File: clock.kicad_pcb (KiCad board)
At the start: 2 copper layers, 51.4 x 38.8 mm, 134 parts, among them J1 USB_C_Receptacle_USB2.0_16P, J3 Conn_01x02_Pin, J4 Conn_01x02_Pin, J5 Battery, Q1 2N7002K, Q2 NPN, SW1 SW_SPST, SW2 SW_SPST, SW4 SW_SPDT, SW5 SW_SPST, U1 STM32F072CBT6, U2 USBLC6-2SC6, U4 MCP73871-2CC, U5 AP2112K-3.3, Y1 8MHz

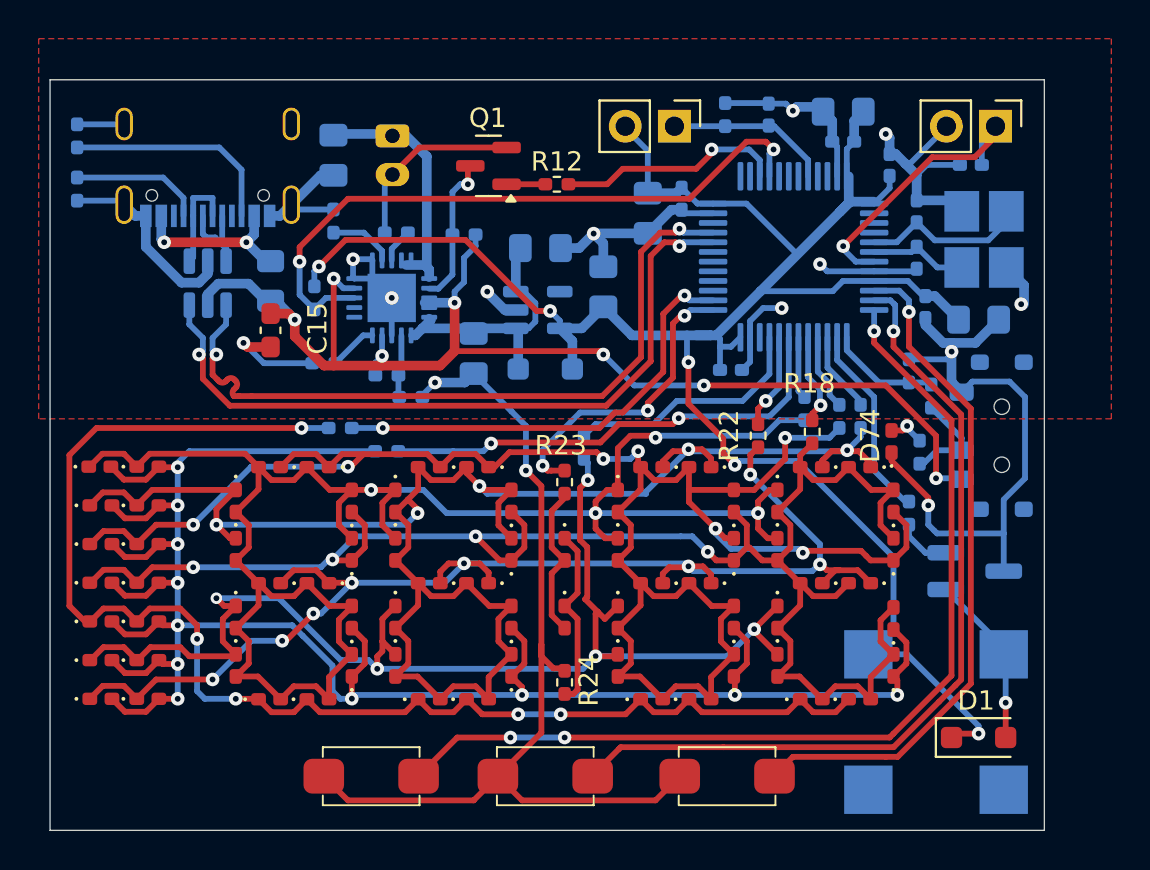
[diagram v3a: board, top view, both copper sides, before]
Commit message: fixed overlap of silkscreen
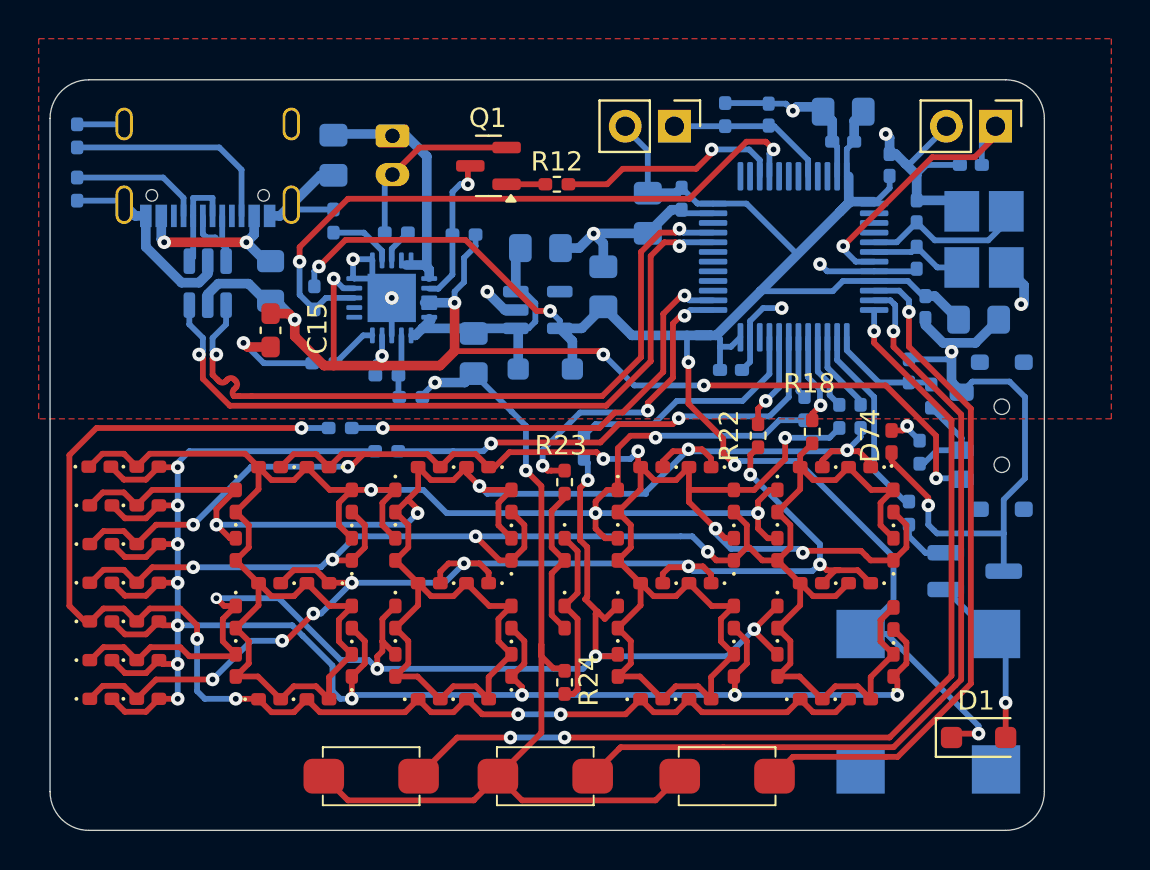
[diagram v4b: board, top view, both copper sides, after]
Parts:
- moved BZ1 1.12 mm to (250.0, 57.8)
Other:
- outline, holes or cut-outs redrawn
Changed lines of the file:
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@@
 		(tags "resistor handsolder")
 		(property "Reference" "R20"
-			(at 3.8 0 360)
+			(at 3.8 0 0)
 			(layer "B.SilkS")
 			(effects
@@
 		)
 		(property "Value" "50R"
-			(at 0 -1.17 360)
+			(at 0 -1.17 0)
 			(layer "B.Fab")
 			(effects
@@
 		)
 		(fp_text user "${REFERENCE}"
-			(at 0 0 360)
+			(at 0 0 0)
 			(layer "B.Fab")
 			(effects
@@
 	(footprint "Buzzer_Beeper:MagneticBuzzer_CUI_CMT-8504-100-SMT"
 		(layer "B.Cu")
-		(at 250.4 58.8 -90)
+		(at 250 57.75 -90)
 		(descr "magnetic transducer buzzer, 5V, SPL of 100 dB at 10 cm, https://www.cuidevices.com/product/resource/pdf/cmt-8504-100-smt-tr.pdf")
 		(tags "CMT 8504")
@@
 		(sheetfile "clock.kicad_sch")
 		(attr smd)
+		(fp_rect
+			(start -3.3 1.35)
+			(end 3.3 -1.35)
+			(stroke
+				(width 0.05)
+				(type default)
+			)
+			(fill none)
+			(layer "B.SilkS")
+		)
+		(fp_rect
+			(start -4.5 3)
+			(end 4.5 -3)
+			(stroke
+				(width 0.05)
+				(type default)
+			)
+			(fill none)
+			(layer "B.CrtYd")
+		)
 		(fp_line
 			(start -0.2 1.35)
@@
 				(type default)
 			)
-			(layer "B.SilkS")
+			(layer "User.1")
 		)
 		(fp_line
@@
 				(type default)
 			)
-			(layer "B.SilkS")
+			(layer "User.1")
 		)
 		(fp_line
@@
 				(type default)
 			)
-			(layer "B.SilkS")
+			(layer "User.1")
 		)
 		(fp_line
@@
 				(type default)
 			)
-			(layer "B.SilkS")
+			(layer "User.1")
 		)
 		(fp_line
@@
 				(type default)
 			)
-			(layer "B.SilkS")
+			(layer "User.1")
 		)
 		(fp_line
@@
 				(type default)
 			)
-			(layer "B.SilkS")
-		)
-		(fp_rect
-			(start -3.3 1.35)
-			(end 3.3 -1.35)
-			(stroke
-				(width 0.05)
-				(type default)
-			)
-			(fill none)
-			(layer "B.SilkS")
-		)
-		(fp_rect
-			(start -4.5 3)
-			(end 4.5 -3)
-			(stroke
-				(width 0.05)
-				(type default)
-			)
-			(fill none)
-			(layer "B.CrtYd")
+			(layer "User.1")
 		)
 		(fp_text user "${REFERENCE}"
@@
 		(tags "USB C Type-C Receptacle USB2.0")
 		(property "Reference" "J1"
-			(at 0 4.58 0)
+			(at 0 4.58 180)
 			(layer "B.SilkS")
 			(hide yes)
@@
 		)
 		(property "Value" "USB_C_Receptacle_USB2.0_16P"
-			(at 0 -6.24 0)
+			(at 0 -6.24 180)
 			(layer "B.Fab")
 			(effects
@@
 		(attr smd)
 		(fp_line
-			(start -4.47 -4.84)
-			(end 4.47 -4.84)
-			(stroke
-				(width 0.12)
-				(type solid)
-			)
-			(layer "B.SilkS")
-		)
-		(fp_line
-			(start -4.47 -3.38)
-			(end -4.47 -4.84)
-			(stroke
-				(width 0.12)
-				(type solid)
-			)
-			(layer "B.SilkS")
-		)
-		(fp_line
 			(start -4.47 -1.13)
 			(end -4.47 0.67)
@@
 		)
 		(fp_line
-			(start 4.47 -3.38)
-			(end 4.47 -4.84)
-			(stroke
-				(width 0.12)
-				(type solid)
-			)
-			(layer "B.SilkS")
-		)
-		(fp_line
 			(start 4.47 -1.13)
 			(end 4.47 0.67)
@@
 		)
 		(fp_text user "PCB Edge"
-			(at 0 -3.43 0)
+			(at 0 -3.43 180)
 			(layer "Dwgs.User")
 			(effects
@@
 		)
 		(fp_text user "${REFERENCE}"
-			(at 0 -1.18 0)
+			(at 0 -1.18 180)
 			(layer "B.Fab")
 			(effects
@@
 		)
 	)
-	(gr_rect
-		(start 204.6 25.6)
-		(end 256 64.4)
+	(gr_arc
+		(start 204.6 27.6)
+		(mid 205.185786 26.185786)
+		(end 206.6 25.6)
+		(stroke
+			(width 0.05)
+			(type default)
+		)
+		(layer "Edge.Cuts")
+	)
+	(gr_line
+		(start 206.6 25.6)
+		(end 254 25.6)
+		(stroke
+			(width 0.05)
+			(type default)
+		)
+		(layer "Edge.Cuts")
+	)
+	(gr_line
+		(start 254 64.4)
+		(end 206.6 64.4)
+		(stroke
+			(width 0.05)
+			(type default)
+		)
+		(layer "Edge.Cuts")
+	)
+	(gr_line
+		(start 256 27.6)
+		(end 256 62.4)
+		(stroke
+			(width 0.05)
+			(type default)
+		)
+		(layer "Edge.Cuts")
+	)
+	(gr_arc
+		(start 254 25.6)
+		(mid 255.414214 26.185786)
+		(end 256 27.6)
+		(stroke
+			(width 0.05)
+			(type default)
+		)
+		(layer "Edge.Cuts")
+	)
+	(gr_arc
+		(start 206.6 64.4)
+		(mid 205.185786 63.814214)
+		(end 204.6 62.4)
+		(stroke
+			(width 0.05)
+			(type default)
+		)
+		(layer "Edge.Cuts")
+	)
+	(gr_line
+		(start 204.6 62.4)
+		(end 204.6 27.6)
+		(stroke
+			(width 0.05)
+			(type default)
+		)
+		(layer "Edge.Cuts")
+	)
+	(gr_arc
+		(start 256 62.4)
+		(mid 255.414214 63.814214)
+		(end 254 64.4)
 		(stroke
 			(width 0.05)
 			(type default)
 		)
-		(fill none)
 		(layer "Edge.Cuts")
 	)
@@
 	)
 	(segment
+		(start 247.85 54.25)
+		(end 252.6 59)
+		(width 0.3)
+		(layer "B.Cu")
+		(net 1)
+	)
+	(segment
 		(start 246.1675 27.72)
 		(end 246.6375 27.25)
@@
 	)
 	(segment
-		(start 248.2 54)
-		(end 246.9 55.3)
-		(width 0.3)
-		(layer "B.Cu")
-		(net 1)
-	)
-	(segment
 		(start 245.061429 36.528521)
 		(end 245.58995 36)
@@
 	)
 	(segment
+		(start 248.2 52.55)
+		(end 246.5 54.25)
+		(width 0.3)
+		(layer "B.Cu")
+		(net 1)
+	)
+	(segment
 		(start 241.328521 36.528521)
 		(end 245.061429 36.528521)
@@
 	)
 	(segment
-		(start 246.9 55.3)
-		(end 248.9 55.3)
+		(start 245.58995 36)
+		(end 247.2 36)
 		(width 0.3)
 		(layer "B.Cu")
@@
 	)
 	(segment
-		(start 245.58995 36)
-		(end 247.2 36)
+		(start 239.8 39.4)
+		(end 240.2875 38.9125)
 		(width 0.3)
 		(layer "B.Cu")
@@
 	)
 	(segment
-		(start 239.8 39.4)
-		(end 240.2875 38.9125)
+		(start 248.2 50.275)
+		(end 248.2 52.55)
 		(width 0.3)
 		(layer "B.Cu")
@@
 	)
 	(segment
-		(start 248.9 55.3)
-		(end 252.6 59)
-		(width 0.3)
-		(layer "B.Cu")
-		(net 1)
-	)
-	(segment
 		(start 238.0675 32)
 		(end 237.25 31.1825)
@@
 	)
 	(segment
-		(start 248.2 50.275)
-		(end 248.2 54)
-		(width 0.3)
+		(start 231.6 40.55)
+		(end 231.6 39.1)
+		(width 0.5)
 		(layer "B.Cu")
 		(net 1)
 	)
 	(segment
-		(start 231.6 40.55)
-		(end 231.6 39.1)
-		(width 0.5)
+		(start 246.5 54.25)
+		(end 247.85 54.25)
+		(width 0.3)
 		(layer "B.Cu")
 		(net 1)
@@
 	)
 	(segment
+		(start 252.6 59)
+		(end 252.6 59.4)
+		(width 0.3)
+		(layer "B.Cu")
+		(net 1)
+	)
+	(segment
 		(start 218.2625 36.2775)
 		(end 218.2625 35.4875)
@@
 	)
 	(segment
-		(start 252.6 59)
-		(end 252.6 59.4)
-		(width 0.3)
-		(layer "B.Cu")
-		(net 1)
-	)
-	(segment
 		(start 247.2 32)
 		(end 248 31.2)
@@
 	)
 	(segment
-		(start 254 55.4)
-		(end 253.9 55.3)
+		(start 253.5 54.25)
+		(end 253.2 54.25)
 		(width 0.3)
 		(layer "B.Cu")
@@
 	)
 	(segment
-		(start 250.9 51.95)
-		(end 253.9 54.95)
+		(start 254 54.75)
+		(end 253.5 54.25)
 		(width 0.3)
 		(layer "B.Cu")
@@
 	)
 	(segment
-		(start 253.9 54.95)
-		(end 253.9 55.3)
+		(start 254 57.8)
+		(end 254 54.75)
 		(width 0.3)
 		(layer "B.Cu")
@@
 	)
 	(segment
-		(start 254 57.8)
-		(end 254 55.4)
+		(start 253.2 54.25)
+		(end 250.9 51.95)
 		(width 0.3)
 		(layer "B.Cu")
@@
 	)
 	(segment
-		(start 251.2 56.4)
-		(end 251.2 43.2)
-		(width 0.3)
-		(layer "F.Cu")
-		(net 65)
-	)
-	(segment
-		(start 231.2 59.6)
-		(end 248 59.6)
+		(start 247.2 39.2)
+		(end 247.2 38.6)
 		(width 0.3)
 		(layer "F.Cu")
@@
 	)
 	(segment
-		(start 248.2 59.4)
-		(end 251.2 56.4)
+		(start 251.2 56.4)
+		(end 251.2 43.2)
 		(width 0.3)
 		(layer "F.Cu")
@@
 	)
 	(segment
-		(start 248 59.6)
-		(end 248.2 59.4)
+		(start 231.2 59.6)
+		(end 248 59.6)
 		(width 0.3)
 		(layer "F.Cu")
@@
 	)
 	(segment
-		(start 247.2 39.2)
-		(end 247.2 38.6)
+		(start 248 59.6)
+		(end 251.2 56.4)
 		(width 0.3)
 		(layer "F.Cu")

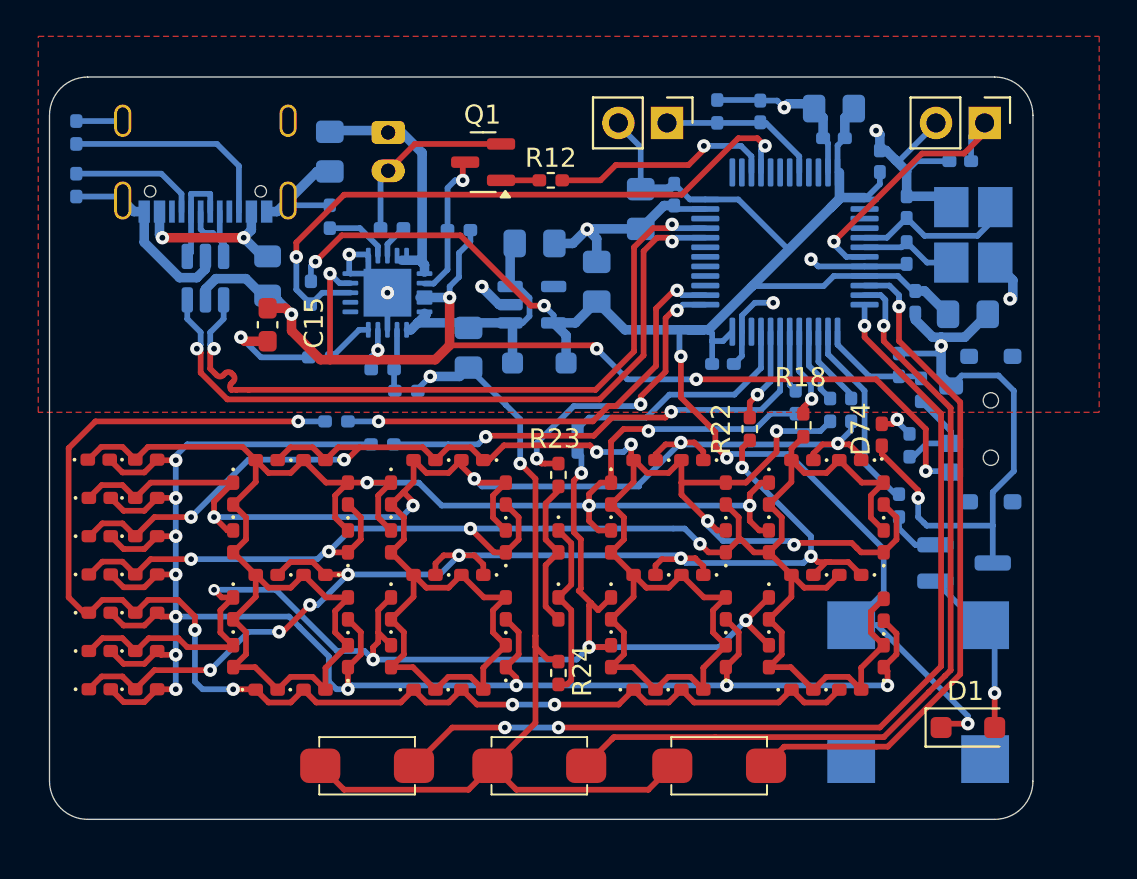
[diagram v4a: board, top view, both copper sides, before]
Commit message: looking good, changed buzzer, changed buzzer pin, changed resistors, changed stcube ide config
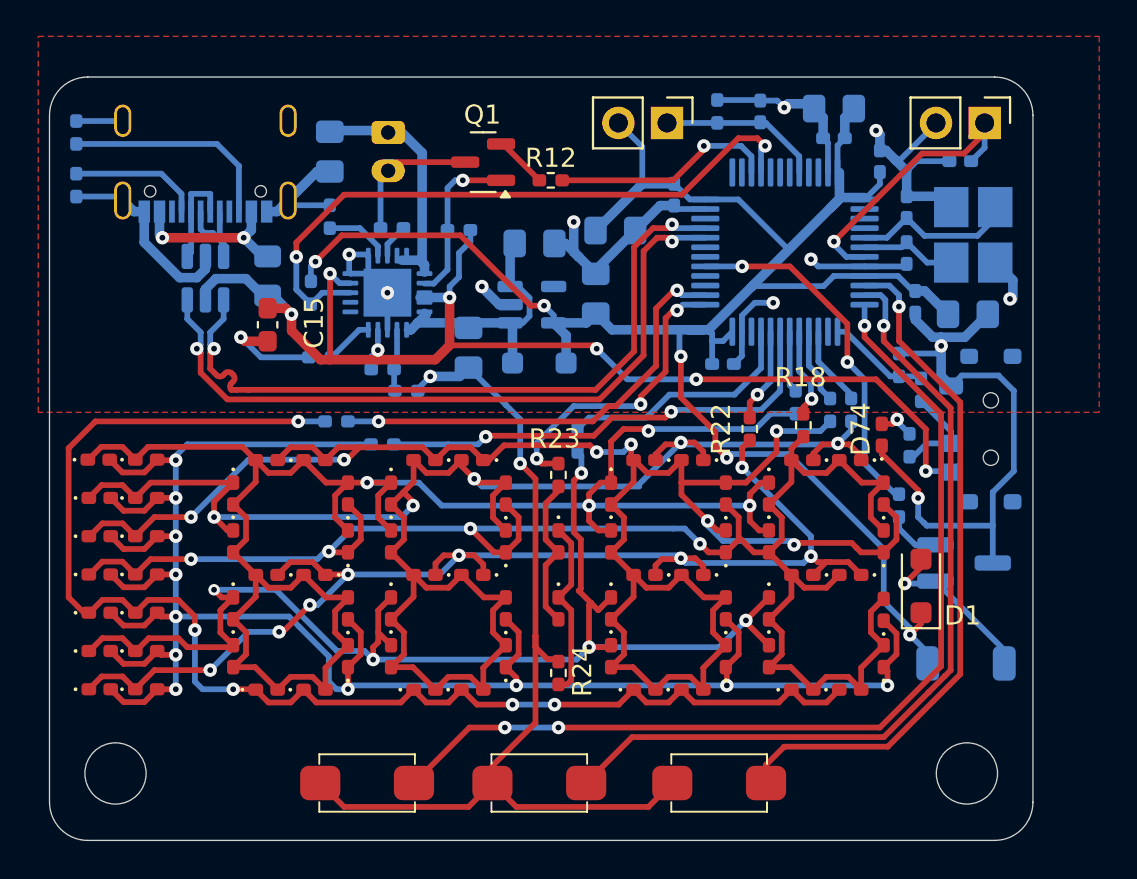
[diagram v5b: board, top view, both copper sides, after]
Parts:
- removed J3: Conn_01x02_Pin, Connector_PinHeader_2.54mm:PinHeader_1x02_P2.54mm_Vertical
- added H1: MountingHole, MountingHole:MountingHole_3.2mm_M3, F.Cu at (208.1, 62.0)
- added H2: MountingHole, MountingHole:MountingHole_3.2mm_M3, F.Cu at (252.6, 62.0)
- added J2: Conn_01x02_Pin, Connector_PinHeader_2.54mm:PinHeader_1x02_P2.54mm_Vertical, F.Cu at (253.5, 28.0)
- BZ1: footprint Buzzer_Beeper:MagneticBuzzer_CUI_CMT-8504-100-SMT -> FB_clock_lib:Buzzer
- Q1: value 2N7002K -> NMOS-SI2302
- R13: value 470R -> 180R
- moved D1 7.80 mm to (250.2, 52.2), turned to 90 degrees
- moved BZ1 2.92 mm to (252.5, 56.2), turned to 0 degrees
- moved C5 1.74 mm to (234.2, 33.6), turned to 0 degrees
- moved SW1 0.90 mm to (230.2, 62.5)
- moved SW2 0.90 mm to (239.6, 62.5)
- moved SW5 0.90 mm to (221.2, 62.5)
- moved C19 0.63 mm to (233.2, 36.9)
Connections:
- Q1 pad 1: Net-(Q1-G) -> Net-(Q1-D)
- Q1 pad 2: GND -> Net-(Q1-G)
- Q1 pad 3: Net-(Q1-D) -> GND
- U1 pad 14: BUZZER -> unconnected-(U1-PA4-Pad14)
- U1 pad 29: unconnected-(U1-PA8-Pad29) -> BUZZER
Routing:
- net BUZZER: track 9.95 -> 18.6 mm, vias 0 -> 2
- net +3.3V: track 111.5 -> 107.6 mm
- net NRST: track 15.1 -> 16.1 mm
- net Net-(Q1-D): track 7.74 -> 8.74 mm
- net RIGHT: track 35.3 -> 36.2 mm
- net GND: track 168.8 -> 169.6 mm
- net Net-(Q1-G): track 2.00 -> 2.79 mm
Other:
- board size 51.4 x 38.8 mm -> 51.4 x 39.9 mm

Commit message: changed resistor values
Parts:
- R5: value 2k -> 1.1k / 500R for 900/1000
- R8: value 100k -> 30k / 20k for 900/1000
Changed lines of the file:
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@@
 		)
 		(fp_text user "${REFERENCE}"
-			(at 0 1.27 360)
+			(at 0 1.27 0)
 			(layer "F.Fab")
 			(effects
@@
 			)
 		)
-		(property "Value" "100k"
+		(property "Value" "30k / 20k for 900/1000"
 			(at 0 -1.17 90)
 			(layer "B.Fab")
@@
 		(tags "capacitor handsolder")
 		(property "Reference" "C5"
-			(at -1.125 -1.625 360)
+			(at -1.125 -1.625 0)
 			(layer "B.SilkS")
 			(effects
@@
 		)
 		(property "Value" "4.7uF"
-			(at 0 -1.68 360)
+			(at 0 -1.68 0)
 			(layer "B.Fab")
 			(effects
@@
 		)
 		(fp_text user "${REFERENCE}"
-			(at 0 0 360)
+			(at 0 0 0)
 			(layer "B.Fab")
 			(effects
@@
 			)
 		)
-		(property "Value" "2k"
+		(property "Value" "1.1k / 500R for 900/1000"
 			(at 0 -1.17 0)
 			(layer "B.Fab")

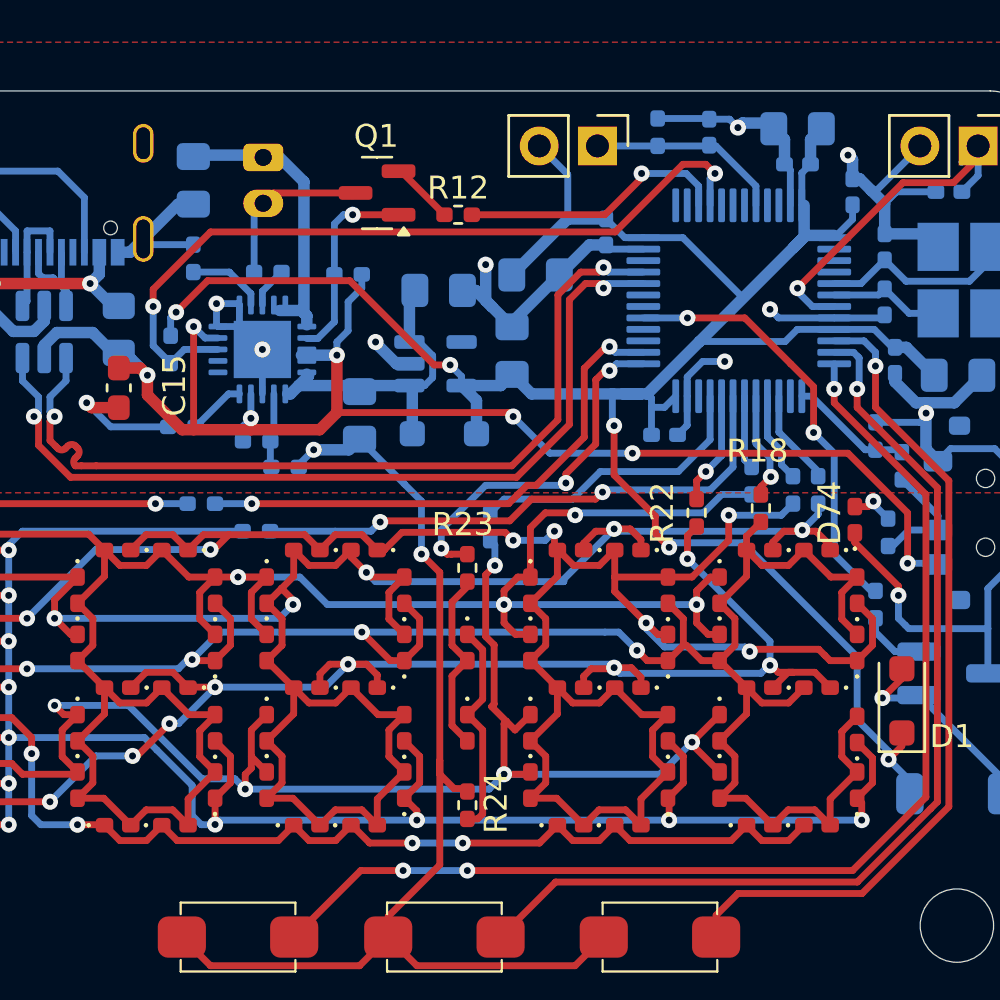
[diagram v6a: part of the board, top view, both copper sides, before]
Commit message: silk screen additions
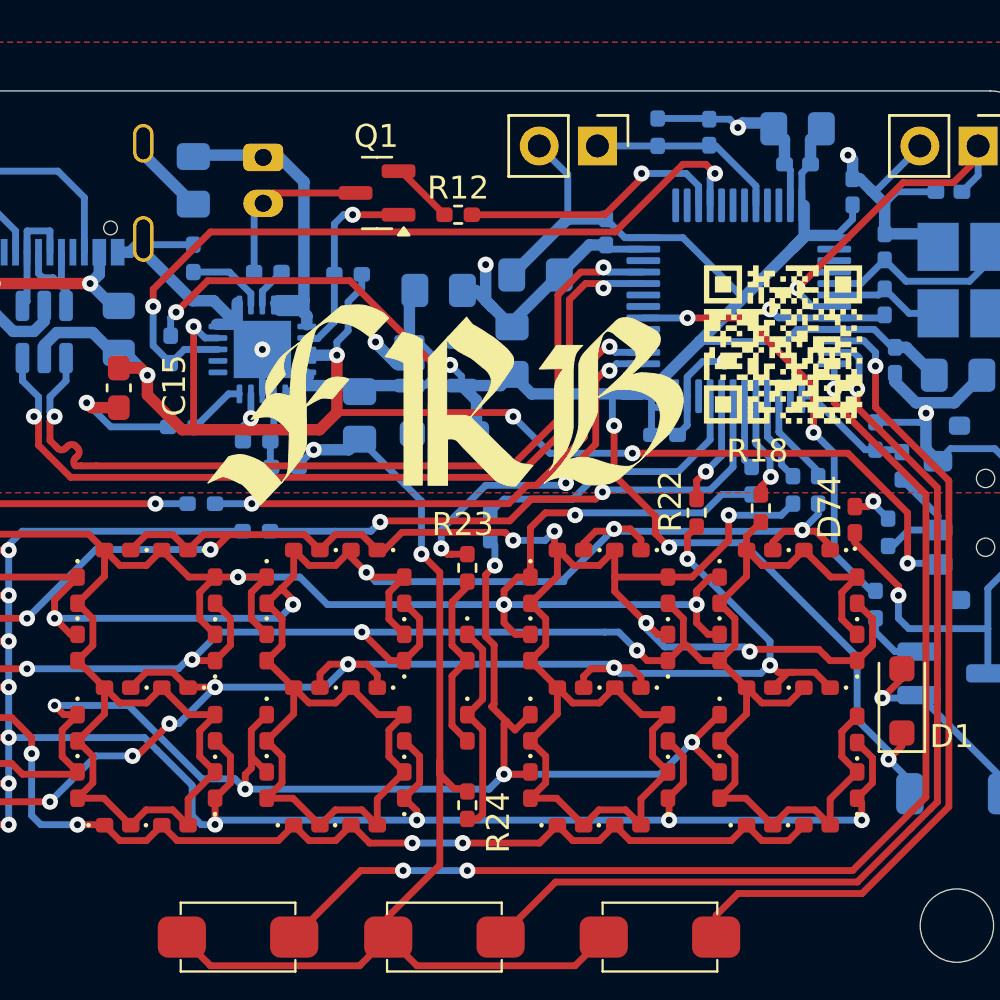
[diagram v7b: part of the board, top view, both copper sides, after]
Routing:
- net GND: track 169.6 -> 175.7 mm, vias 14 -> 13
- net /BAT: track 12.7 -> 14.0 mm
